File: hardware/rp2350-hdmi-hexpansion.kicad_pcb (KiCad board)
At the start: 4 copper layers, 47.3 x 54.3 mm, 60 parts, among them J1 Hexpansion-Connector, J3 SWD, J4 Qwiic, J5 HDMI-A, SW3 RESET, U1 RP2354A, U11 SN74LVC1G07, U4 TPS61023DRLR, U6 TPD4E05U06, U7 TPD4E05U06, Y1 12MHz

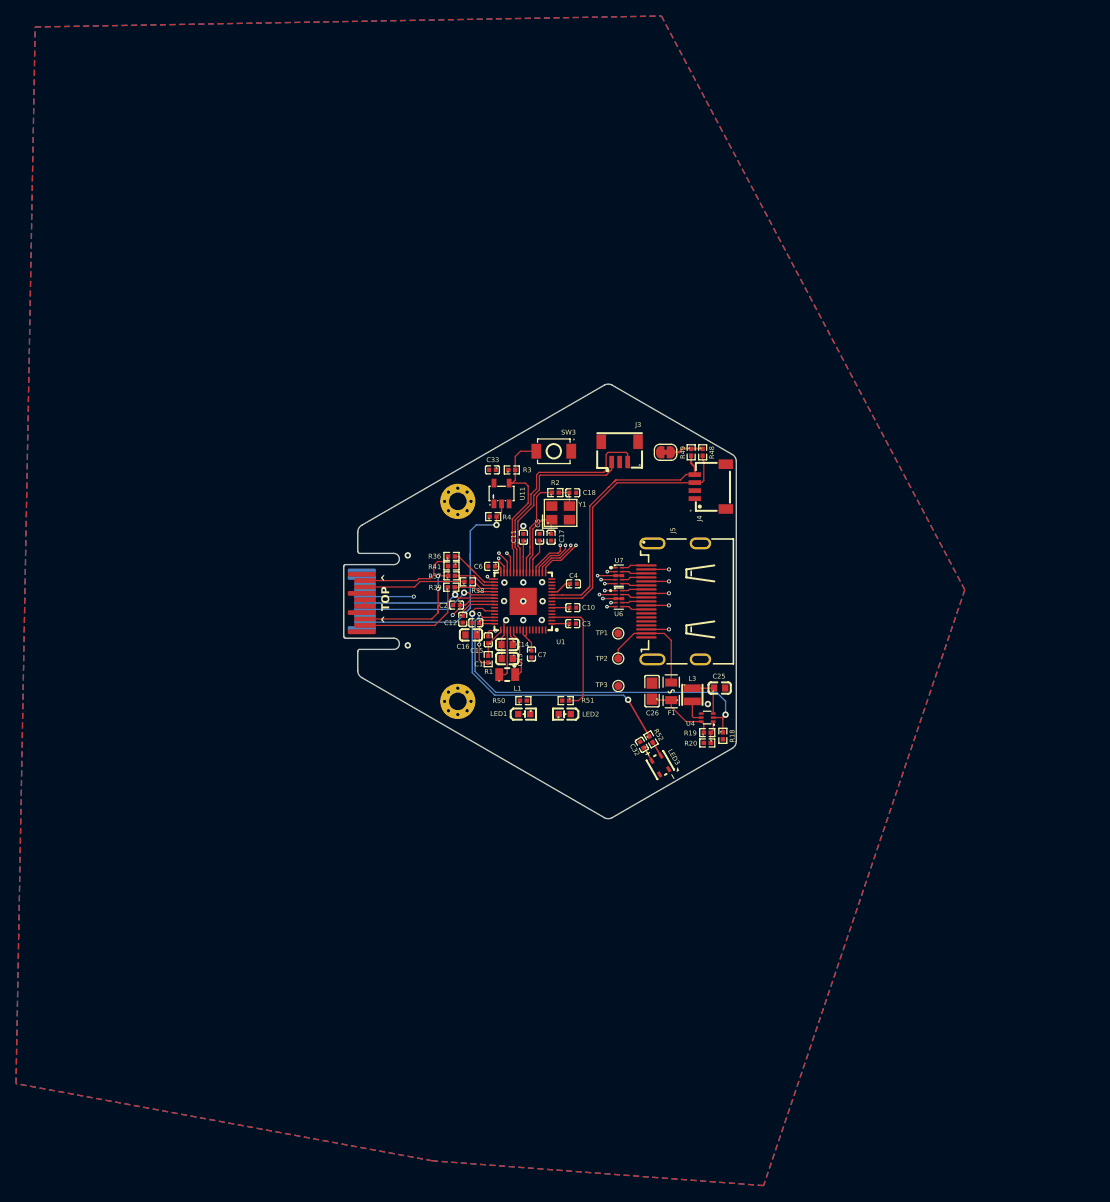
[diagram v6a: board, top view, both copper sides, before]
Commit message: hardware: merge 3V3_BADGE into +3V3, ignore hardware/reference, save PCB layout
Co-Authored-By: Claude Sonnet 5.5 <noreply@anthropic.com>
Claude-Session: https://claude.ai/code/session_01VMD2iSg4JfioYFvgvvdo7j
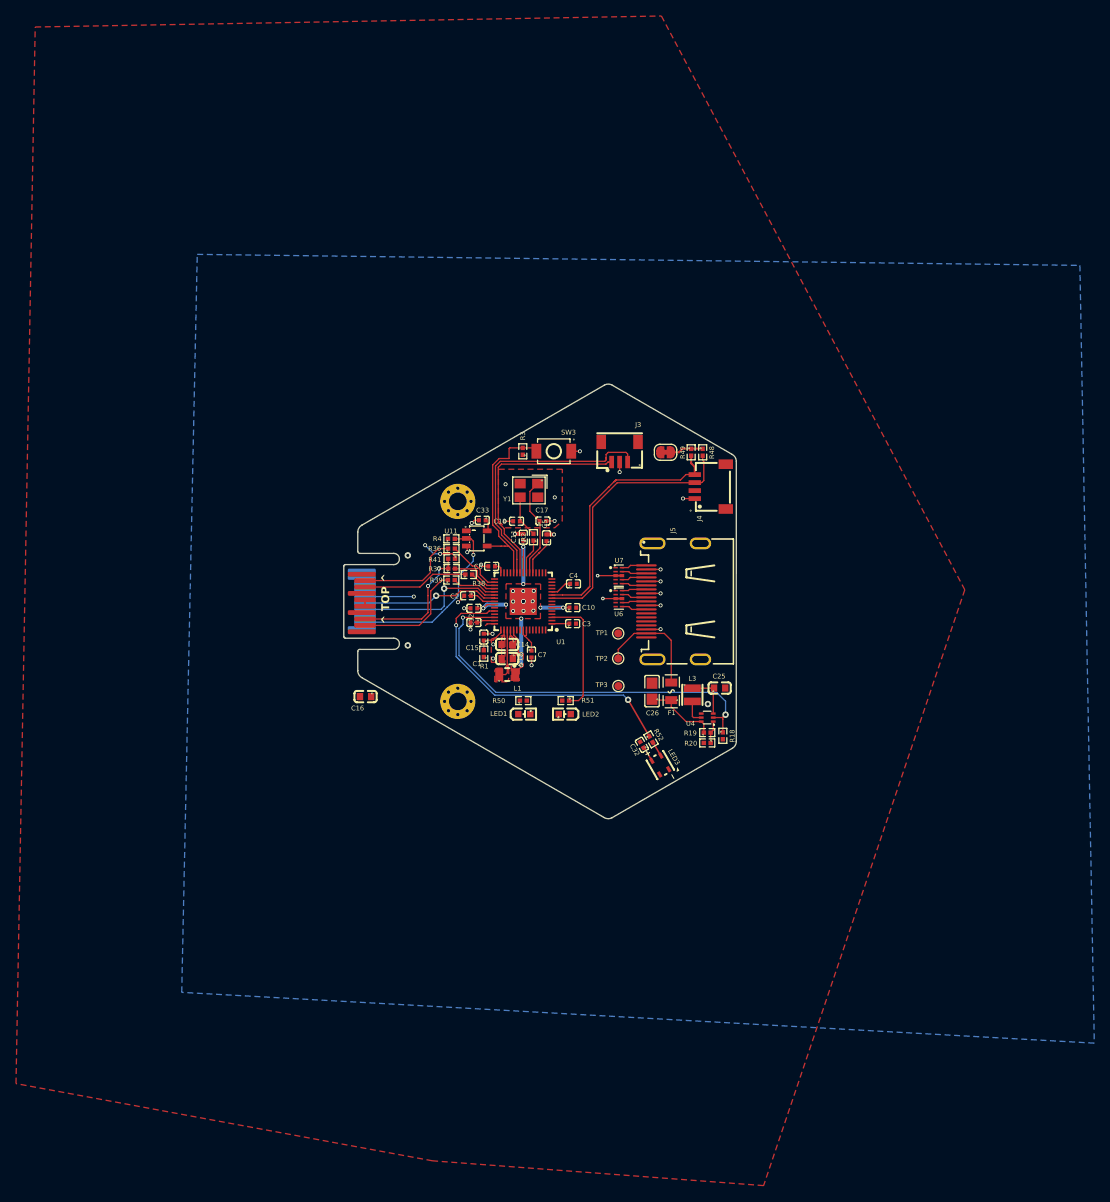
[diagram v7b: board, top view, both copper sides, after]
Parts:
- moved C16 15.3 mm to (101.0, 111.9)
- moved C18 7.88 mm to (119.8, 90.0), turned to 180 degrees
- moved C33 6.43 mm to (115.6, 89.9)
- moved U11 6.42 mm to (114.9, 92.1), turned to 180 degrees
- moved R2 6.20 mm to (122.0, 92.0), turned to 90 degrees
- moved R4 5.91 mm to (111.7, 92.2)
- moved Y1 4.86 mm to (121.4, 86.1), turned to 180 degrees
- moved R3 2.70 mm to (120.6, 81.2), turned to 90 degrees
- moved C17 2.27 mm to (123.1, 90.0), turned to 0 degrees
- moved C12 1.95 mm to (114.5, 100.9), turned to 180 degrees
- moved C2 1.81 mm to (113.7, 99.3)
- moved R36 0.98 mm to (111.7, 93.4)
- moved R38 0.92 mm to (113.9, 96.6)
- moved R39 0.90 mm to (111.7, 97.3)
- moved R37 0.90 mm to (111.7, 95.9)
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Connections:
- C33 pad 1: /3V3_BADGE -> +3V3
- J1 pad 15: /3V3_BADGE -> +3V3
- J1 pad 16: /3V3_BADGE -> +3V3
- R4 pad 1: /3V3_BADGE -> +3V3
- R41 pad 1: /3V3_BADGE -> +3V3
- U11 pad 5: /3V3_BADGE -> +3V3
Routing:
- net /HDMI_D0_N: track 25.2 -> 3.19 mm, vias 2 -> 0
- net /HDMI_D1_N: track 23.9 -> 3.14 mm, vias 2 -> 0
- net /HDMI_D0_P: track 22.9 -> 3.10 mm, vias 2 -> 0
- net /HDMI_D1_P: track 22.2 -> 3.17 mm, vias 2 -> 0
- net /HDMI_CK_N: track 21.8 -> 3.19 mm, vias 2 -> 0
- net /HDMI_CK_P: track 20.6 -> 3.10 mm, vias 2 -> 0
- net /HDMI_D2_N: track 16.4 -> 3.14 mm, vias 2 -> 0
- net /HDMI_D2_P: track 15.7 -> 3.17 mm, vias 2 -> 0
- net /DVDD: track 18.4 -> 28.3 mm, vias 0 -> 9
- net /XOUT: track 12.2 -> 4.37 mm
- net /LS_A: track 30.8 -> 23.1 mm
- net GND: track 32.2 -> 39.8 mm, vias 22 -> 49
- net /SWCLK: track 23.7 -> 28.8 mm
- net /SWDIO: track 28.2 -> 33.2 mm
- net /RUN: track 21.0 -> 24.4 mm
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- added copper zone on F.Cu, net +3V3
- added copper zone on F.Cu, net /DVDD
- added copper zone on F.Cu, net /VREG_LX

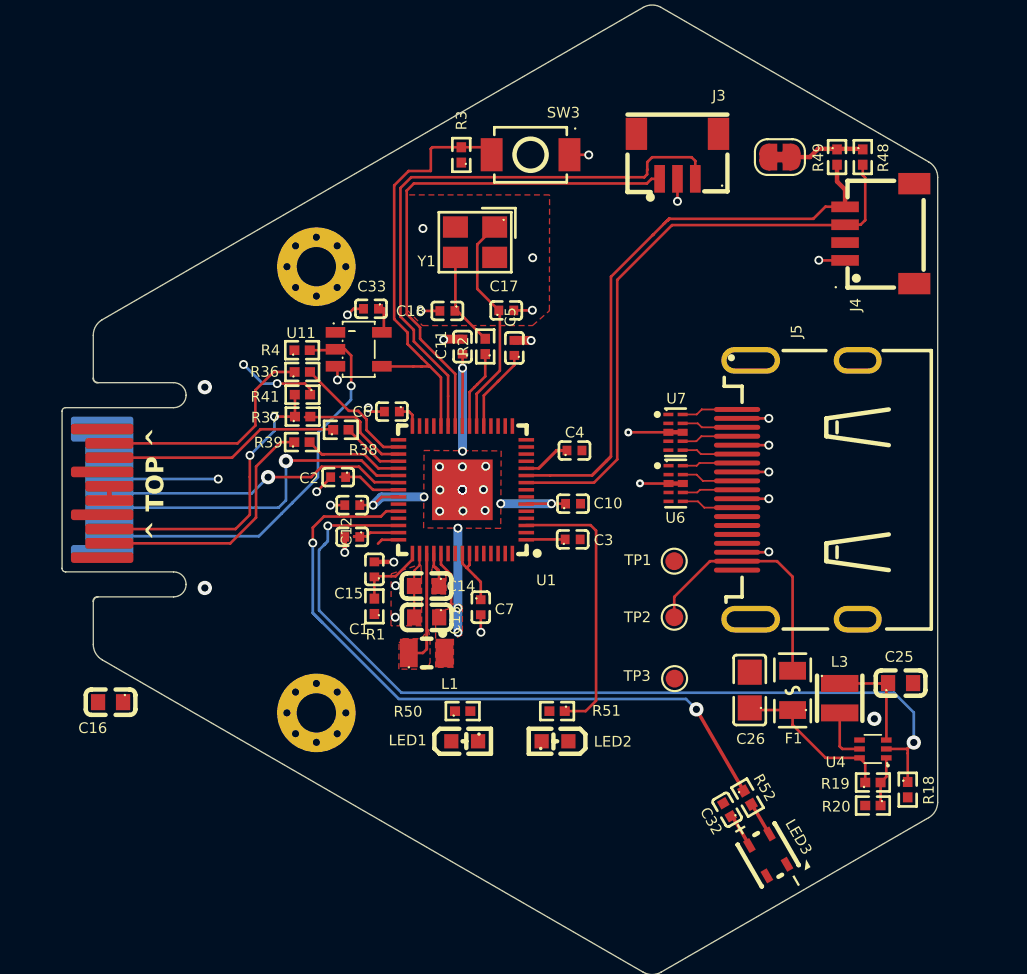
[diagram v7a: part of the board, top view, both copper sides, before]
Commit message: hardware: drop U11/C33/R4, add R53 LS_A-RUN link, update PCB and BOM
Co-Authored-By: Claude Sonnet 5.5 <noreply@anthropic.com>
Claude-Session: https://claude.ai/code/session_01VMD2iSg4JfioYFvgvvdo7j
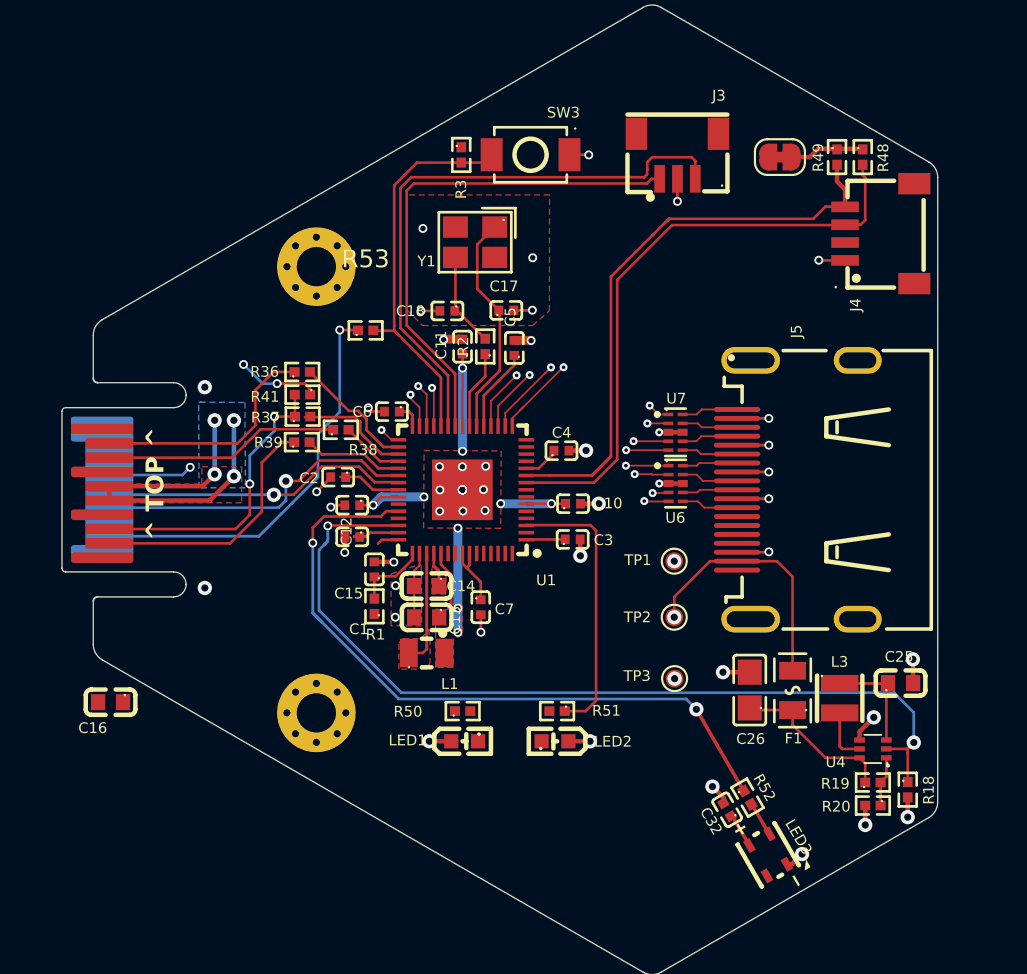
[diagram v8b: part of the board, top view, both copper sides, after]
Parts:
- removed C33: 100nF, jlc:C0402
- removed R4: 10k, jlc:R0402
- removed U11: SN74LVC1G07, jlc:SOT-23-5_L3.0-W1.7-P0.95-LS2.8-BR
- added R53: 1k, jlc:R0402, F.Cu at (115.3, 91.1)
- moved C4 0.73 mm to (126.2, 97.8)
- turned R3 to -90 degrees
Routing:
- net /HDMI_D0_N: track 3.19 -> 23.9 mm, vias 0 -> 2
- net /HDMI_D0_P: track 3.10 -> 22.6 mm, vias 0 -> 2
- net /HDMI_D1_N: track 3.14 -> 22.1 mm, vias 0 -> 2
- net +3V3: track 36.7 -> 54.6 mm, vias 2 -> 7
- net /HDMI_D1_P: track 3.17 -> 20.7 mm, vias 0 -> 2
- net /HDMI_CK_N: track 3.19 -> 20.6 mm, vias 0 -> 2
- net /HDMI_CK_P: track 3.10 -> 19.5 mm, vias 0 -> 2
- net /HDMI_D2_N: track 3.14 -> 15.8 mm, vias 0 -> 2
- net /HDMI_D2_P: track 3.17 -> 14.9 mm, vias 0 -> 2
- net GND: track 39.8 -> 48.2 mm, vias 49 -> 59
- net /RUN: track 24.4 -> 22.2 mm
- net /BADGE_SDA: track 18.9 -> 18.3 mm
- net /V5_HDMI: vias 0 -> 1
- added copper zone on B.Cu, net +3V3
